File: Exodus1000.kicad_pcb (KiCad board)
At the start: 4 copper layers, 147.3 x 64.5 mm, 93 parts, among them J1 ARJ-169, J2 USB_B_Mini, J3 Conn_01x02, M1 ET60S-02-24-02-X-VP-GP, M2 ET60S-02-24-02-X-VP-GP, M3 ET60S-02-24-02-X-VP-GP, M4 ET60S-02-24-02-X-VP-GP, U1 TM4C1294NCPDTGOOD, U2 93LCxxB, U3 FT232H, U4 tusb2077a, U5 IS42S16400J-xC, U6 74LS125, Y1 Crystal_GND24, Y2 Crystal_GND24, Y3 Crystal_GND24

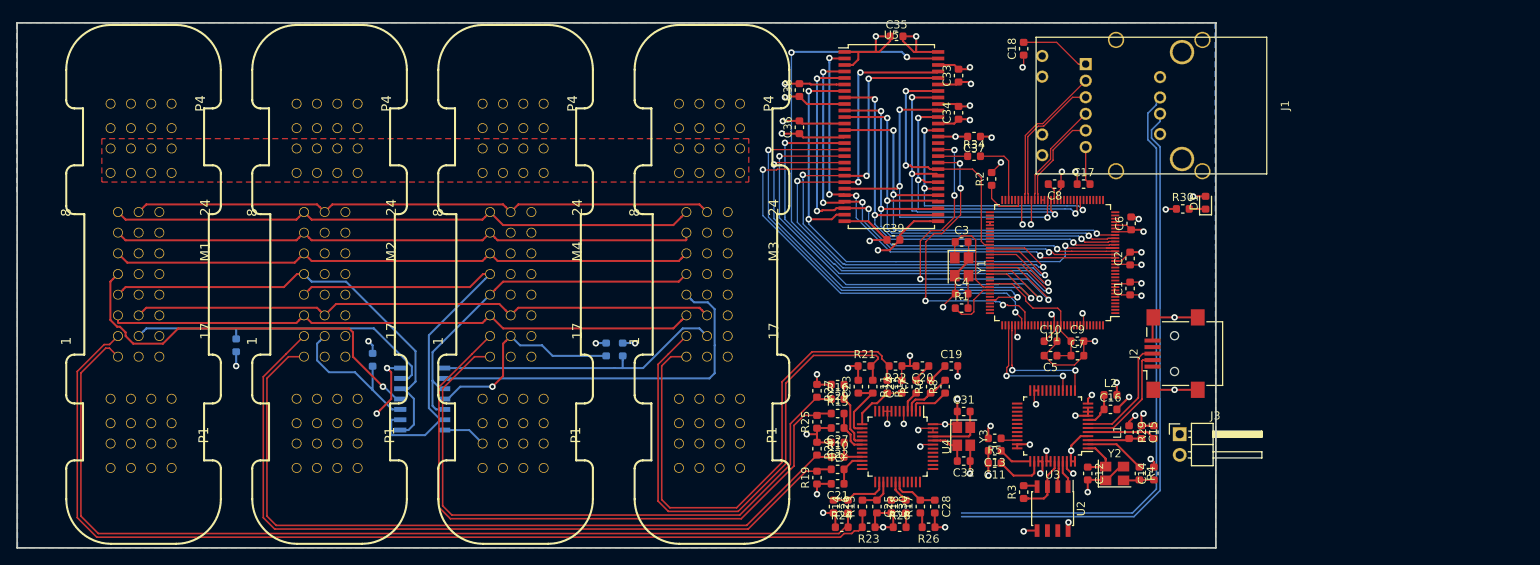
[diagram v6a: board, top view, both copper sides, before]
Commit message: layout done sans connector. It's pretty big. Likely going to need to tear some of this up.
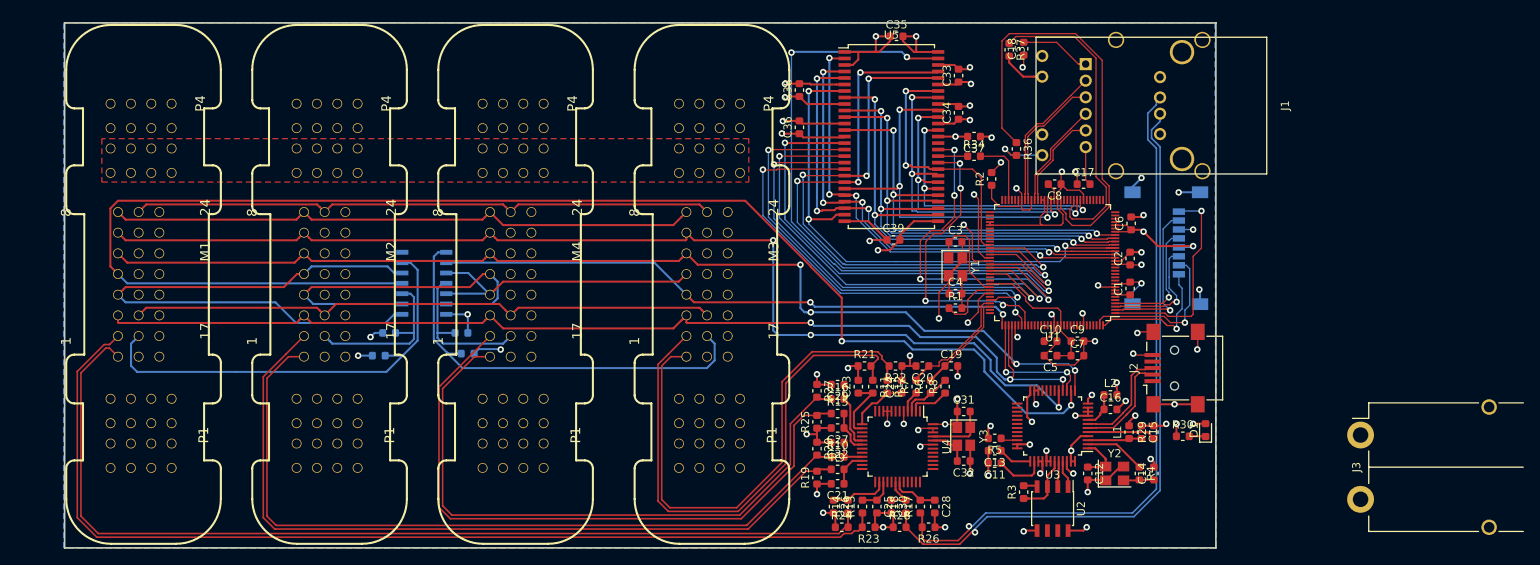
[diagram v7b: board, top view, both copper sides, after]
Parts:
- added J4: Micro_SD_Card, Connector_Card:microSD_HC_Wuerth_693072010801, B.Cu at (183.1, 94.0)
- added R36: R_Small, Resistor_SMD:R_0603_1608Metric, F.Cu at (164.7, 81.8)
- added R37: R_Small, Resistor_SMD:R_0603_1608Metric, F.Cu at (163.8, 69.6)
- J3: footprint Connector_PinHeader_2.54mm:PinHeader_1x02_P2.54mm_Horizontal -> Exodus_Connectors:Anderson_PP15_1x2_RightAngle
- moved D1 27.9 mm to (188.0, 116.3)
- moved R30 27.9 mm to (185.2, 117.1)
- moved J3 22.2 mm to (207.0, 116.9), turned to 270 degrees
- moved R33 19.1 mm to (97.3, 106.9), turned to 0 degrees
- moved R35 17.9 mm to (96.5, 104.4), turned to 0 degrees
- moved R31 17.6 mm to (86.4, 107.2), turned to 180 degrees
- moved U6 14.2 mm to (91.9, 98.3)
- moved R32 3.88 mm to (87.6, 104.4), turned to 180 degrees
- moved J2 1.78 mm to (184.2, 108.7)
- moved C3 0.76 mm to (157.2, 93.2)
- moved C4 0.76 mm to (157.2, 99.6)
- moved R1 0.76 mm to (157.2, 101.3)
- moved Y1 0.76 mm to (157.2, 96.3)
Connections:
- J1 pad 13: Net-(J1-Pad13) -> GND
- J1 pad 15: Net-(J1-Pad15) -> GND
- U1 pad 1: Net-(U1-Pad1) -> /Connectors/SPI_MISO
- U1 pad 127: Net-(U1-Pad127) -> /Connectors/SPI_DAT3
- U1 pad 128: Net-(U1-Pad128) -> /Connectors/SPI_DAT2
- U1 pad 2: Net-(U1-Pad2) -> /Connectors/SPI_MOSI
- U1 pad 3: Net-(U1-Pad3) -> /Connectors/SPI_SS
- U1 pad 4: Net-(U1-Pad4) -> /Connectors/SPI_SCLK
- U1 pad 42: Net-(U1-Pad42) -> /Connectors/ETH_LED0
- U1 pad 46: Net-(U1-Pad46) -> /Connectors/ETH_LED1
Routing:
- net /Connectors/JTAG_TDO_4: track 49.2 -> 179.4 mm, vias 1 -> 2
- net /Connectors/~JTAG_TRST: track 72.7 -> 136.7 mm, vias 0 -> 3
- net /Connectors/ETH_LED1: track 0.00 -> 54.8 mm
- net /JTAG_TCK: track 88.1 -> 137.4 mm, vias 2 -> 4
- net /JTAG_TMS: track 88.3 -> 132.8 mm, vias 2 -> 3
- net +3V3: track 96.4 -> 137.4 mm, vias 25 -> 27
- net /Connectors/ETH_LED0: track 0.00 -> 38.3 mm
- net /JTAG_TDO: track 45.6 -> 72.5 mm, vias 0 -> 2
- net /Connectors/SPI_MISO: track 0.00 -> 25.8 mm, vias 0 -> 1
- net /Connectors/SPI_DAT3: track 0.00 -> 20.0 mm, vias 0 -> 1
- net GND: track 197.5 -> 217.2 mm, vias 49 -> 55
- net /Connectors/SPI_MOSI: track 0.00 -> 19.6 mm, vias 0 -> 1
- net /Connectors/JTAG_TDO_3: track 54.9 -> 73.5 mm
- net /Connectors/SPI_DAT2: track 0.00 -> 17.3 mm, vias 0 -> 1
- net /Connectors/BOARD_SENSE_1: track 36.2 -> 53.5 mm
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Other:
- board size 147.3 x 64.5 mm -> 141.5 x 64.5 mm

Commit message: some layout
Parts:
- C11, C13, C15, C19, C20, C21, C22, C23, C24, C25, C26, C27, C28, C29, C30, L1, R3, U2: moved to B.Cu
- moved J3 35.2 mm to (171.8, 118.0)
- moved D1 23.4 mm to (188.0, 93.0)
- moved R26 22.6 mm to (155.0, 105.7), turned to 0 degrees
- moved R30 21.0 mm to (188.0, 96.3), turned to 90 degrees
- moved C32 20.1 mm to (149.4, 102.1), turned to 270 degrees
- moved Y3 19.1 mm to (146.3, 102.1), turned to 0 degrees
- moved C31 19.1 mm to (143.3, 102.1), turned to 90 degrees
- moved R17 18.4 mm to (155.0, 107.4), turned to 180 degrees
- moved C28 18.3 mm to (155.0, 107.4), turned to 0 degrees
- moved R28 17.9 mm to (154.9, 111.0)
- moved R23 17.6 mm to (155.0, 112.8), turned to 0 degrees
- moved C30 17.4 mm to (155.0, 109.2), turned to 0 degrees
- moved R8 17.1 mm to (140.2, 104.4), turned to 180 degrees
- moved R18 16.9 mm to (155.0, 109.2), turned to 180 degrees
- moved C19 16.6 mm to (140.2, 106.2)
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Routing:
- net /JTAG_TDO: track 72.5 -> 31.1 mm, vias 2 -> 0
- net GND: track 217.2 -> 250.6 mm, vias 55 -> 42
- net /Connectors/D4_N: track 121.1 -> 150.1 mm
- net /Connectors/D4_P: track 124.5 -> 153.1 mm
- net /JTAG_TMS: track 132.8 -> 158.0 mm
- net /JTAG_TCK: track 137.4 -> 162.2 mm, vias 4 -> 1
- net /Connectors/D5_N: track 84.3 -> 63.9 mm
- net /Connectors/~JTAG_TRST: track 136.7 -> 156.0 mm, vias 3 -> 1
- net /Connectors/D5_P: track 84.4 -> 65.2 mm
- net /Connectors/D3_P: track 97.8 -> 114.1 mm
- net /Connectors/D3_N: track 96.1 -> 111.0 mm
- net /Connectors/JTAG_TDO_4: track 179.4 -> 192.1 mm, vias 2 -> 1
- net /Connectors/D1_N: track 64.8 -> 52.9 mm
- net /Connectors/D1_P: track 66.4 -> 54.7 mm
- net /JTAG_TDI: track 15.9 -> 4.91 mm, vias 2 -> 0
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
